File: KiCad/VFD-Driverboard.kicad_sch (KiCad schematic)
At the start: 27 parts, among them J1 MCU, J2 Breadboard, U1 MC34063AD, U2 LM4871MX_NOPB

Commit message: new PCB
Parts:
- removed J2: Breadboard, Connector_PinHeader_2.54mm:PinHeader_1x10_P2.54mm_Vertical, symbol Connector:Conn_01x10_Pin
- added C9: 82p, Capacitor_SMD:C_1206_3216Metric_Pad1.33x1.80mm_HandSolder, symbol Device:C
- added D3: D, Diode_SMD:D_2010_5025Metric_Pad1.52x2.65mm_HandSolder, symbol Device:D
- added H1, H2, H3, H4: MountingHole, MountingHole:MountingHole_3.2mm_M3_ISO14580_Pad_TopBottom, symbol Mechanical:MountingHole
- added R12: 8k2, Resistor_SMD:R_1206_3216Metric_Pad1.30x1.75mm_HandSolder, symbol Device:R
- added TP1: Vee, TestPoint:TestPoint_Pad_D2.5mm, symbol Connector:TestPoint
- added TP2: F-, TestPoint:TestPoint_Pad_D2.5mm, symbol Connector:TestPoint
- added TP3: F+, TestPoint:TestPoint_Pad_D2.5mm, symbol Connector:TestPoint
- C1, C3, C4, C5: footprint Capacitor_THT:C_Disc_D4.3mm_W1.9mm_P5.00mm -> Capacitor_SMD:C_2220_5750Metric_Pad1.97x5.40mm_HandSolder
- C2, C7: footprint Capacitor_THT:C_Disc_D4.3mm_W1.9mm_P5.00mm -> Capacitor_SMD:C_1206_3216Metric_Pad1.33x1.80mm_HandSolder
- C6, C8: footprint Capacitor_THT:CP_Axial_L10.0mm_D4.5mm_P15.00mm_Horizontal -> Capacitor_Tantalum_SMD:CP_EIA-7343-31_Kemet-D_Pad2.25x2.55mm_HandSolder
- D1: footprint Diode_THT:D_DO-34_SOD68_P7.62mm_Horizontal -> Diode_SMD:D_2010_5025Metric_Pad1.52x2.65mm_HandSolder
- D2: footprint Diode_THT:D_DO-34_SOD68_P7.62mm_Horizontal -> Diode_SMD:D_SOD-123
- L1: footprint Inductor_THT:L_Axial_L5.3mm_D2.2mm_P2.54mm_Vertical_Vishay_IM-1 -> MyLib:IND_TAIYO_NRS8040_TAY
- R1, R10, R11, R2, R3, R4, R5, R6, R9: footprint Resistor_THT:R_Axial_DIN0207_L6.3mm_D2.5mm_P10.16mm_Horizontal -> Resistor_SMD:R_1206_3216Metric_Pad1.30x1.75mm_HandSolder
- R7: value R -> 100k; footprint Resistor_THT:R_Axial_DIN0207_L6.3mm_D2.5mm_P10.16mm_Horizontal -> Resistor_SMD:R_1206_3216Metric_Pad1.30x1.75mm_HandSolder
- R8: value 0,22 -> 1; footprint Resistor_THT:R_Axial_DIN0204_L3.6mm_D1.6mm_P2.54mm_Vertical -> Resistor_SMD:R_1206_3216Metric_Pad1.30x1.75mm_HandSolder
- U1, U2: footprint Package_DIP:DIP-8_W7.62mm -> MyLib:SOIC127P599X175-8N
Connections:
- net GNDD: now also C9.1, D3.2 (A); no longer C1.2, C2.2, C5.2, R2.2, R7.2, U2.1 (SHUTDOWN), U2.7 (GND)
- net VCC: now also R12.2
- net VEE: now also TP1.1
- net VF1: now also TP2.1
- net VF2: now also TP3.1
- net at J1.4 (Pin_4), V1.8 (OSC0): now also C9.2, R12.1
- new net: C1.2, C2.2, C5.2, D3.1 (K), R2.2, R7.2, U2.1 (SHUTDOWN), U2.7 (GND)
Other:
- company: (C) Karl -> KARL
- moved on the sheet: C6, C7, C8, D2, J1, L1, R1, R10, R11, R2, R8, R9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

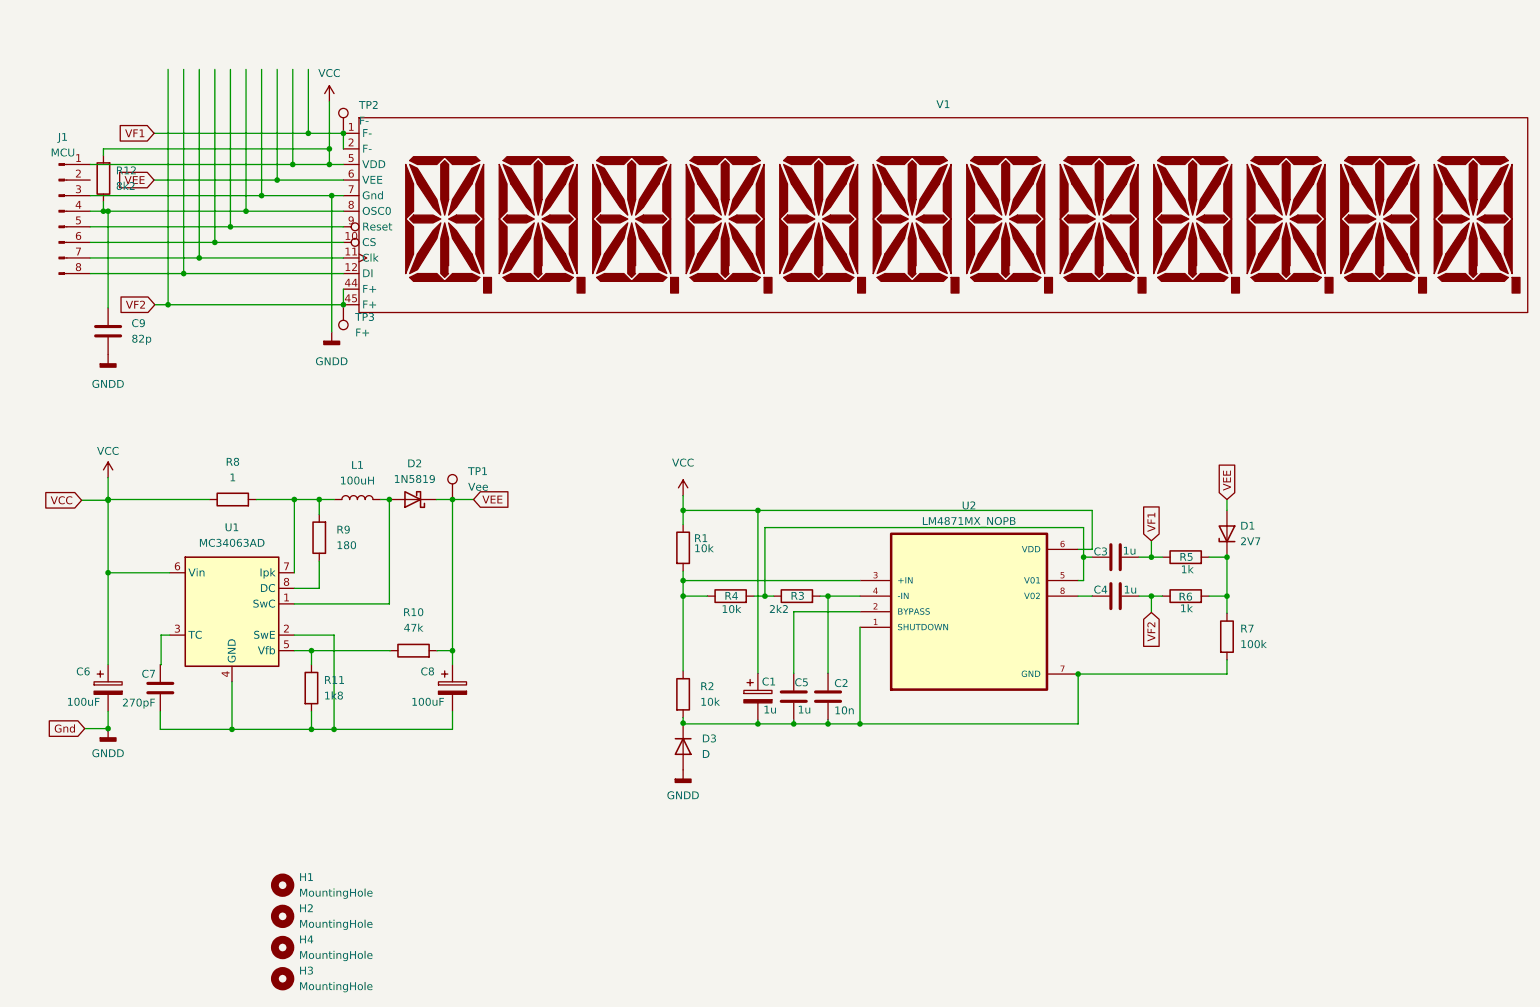
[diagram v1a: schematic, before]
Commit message: added MPLAB project
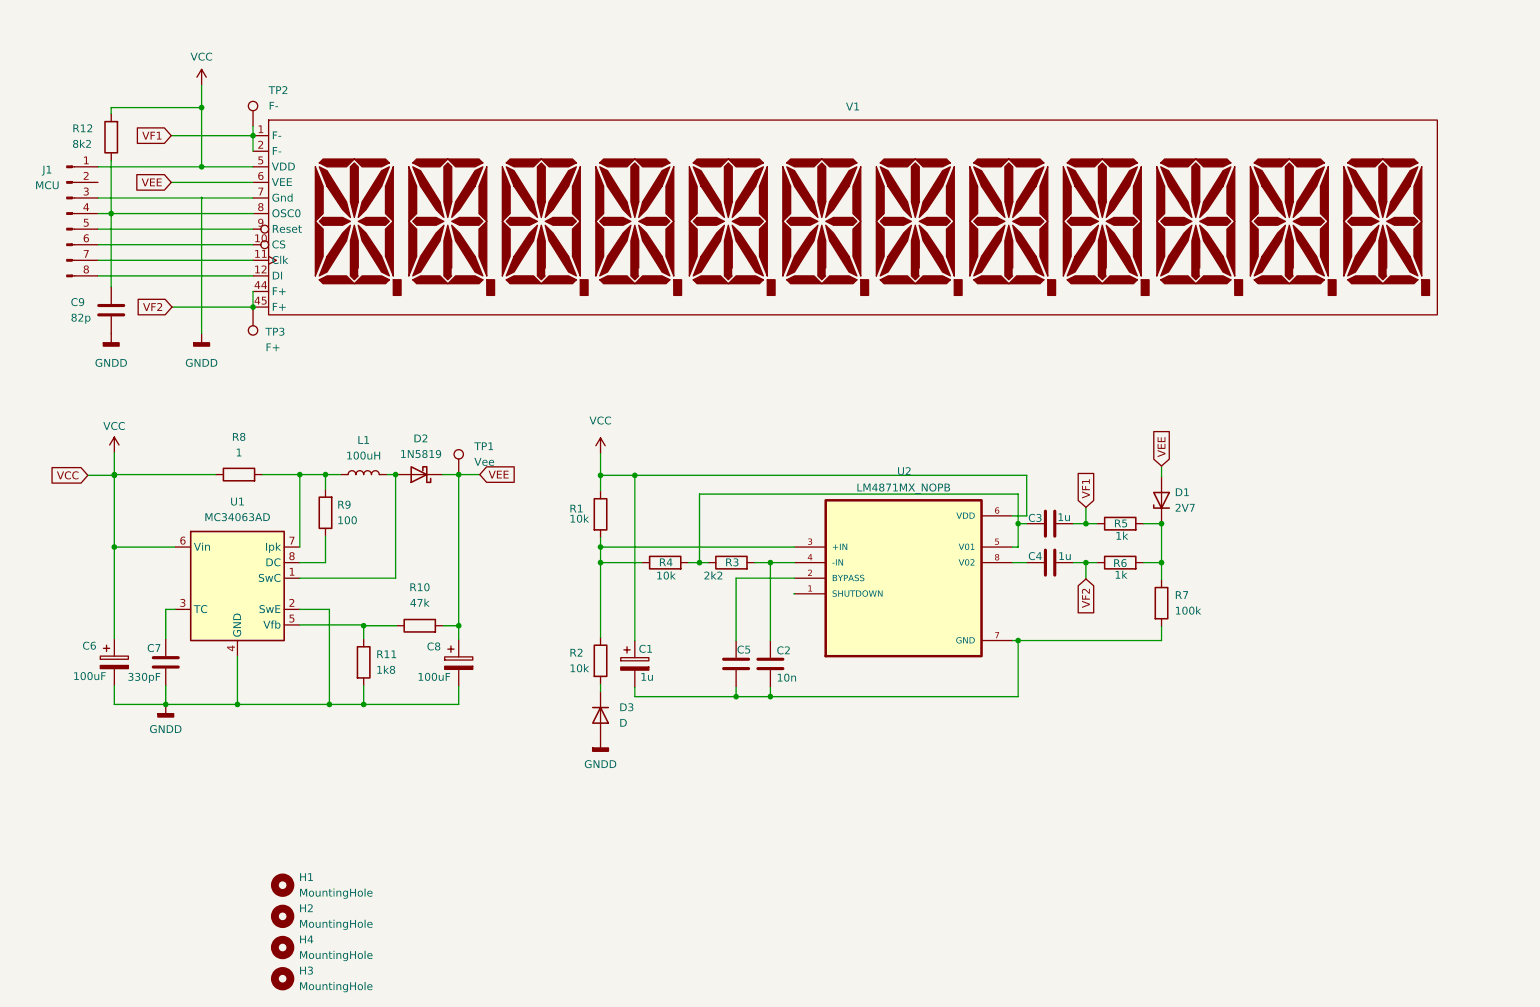
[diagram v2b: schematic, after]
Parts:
- C7: value 270pF -> 330pF
- R9: value 180 -> 100
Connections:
- net GNDD: now also C7.2, C8.2, R11.2, U1.2 (SwE), U1.4 (GND); no longer J1.3 (Pin_3), V1.7 (Gnd)
- net at C1.2, C2.2, C5.2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: no longer D3.1 (K), R2.2, U2.1 (SHUTDOWN)
- new net: J1.3 (Pin_3), V1.7 (Gnd)
- new net: D3.1 (K), R2.2
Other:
- company: KARL -> © rlnd
- moved on the sheet: C1, C2, C3, C4, C5, C6, C7, C8, C9, D1, D2, D3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
